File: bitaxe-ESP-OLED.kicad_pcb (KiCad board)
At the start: 2 copper layers, 57.4 x 42 mm, 48 parts, among them J1 SFV30R-4STE1HLF, J2 Conn_01x06, J3 USB_C_Receptacle_USB2.0_16P, Q1 SI2307, SW1 SWITCH-SPST, SW2 SWITCH-SPST, SW3 SWITCH-SPST, SW4 SWITCH-SPST, U1 ESP32_S3R8, U2 RT9080-33GJ5, U3 AP2502KTR-G1, U4 W25Q128JV

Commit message: very rough routing
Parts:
- moved C2 44.0 mm to (146.6, 76.7), turned to 0 degrees
- moved C21 42.5 mm to (161.7, 73.5)
- moved C13 41.6 mm to (161.7, 71.4)
- moved C3 41.3 mm to (142.8, 75.2)
- moved L1 41.2 mm to (150.6, 82.8), turned to 0 degrees
- moved C19 41.1 mm to (166.2, 72.0), turned to -90 degrees
- moved C18 39.0 mm to (165.0, 72.0), turned to 90 degrees
- moved C17 36.9 mm to (164.0, 72.0), turned to -90 degrees
- moved R1 36.1 mm to (150.1, 73.6), turned to 0 degrees
- moved C11 32.3 mm to (150.5, 81.4)
- moved R5 31.8 mm to (134.7, 89.3)
- moved C1 31.2 mm to (146.7, 79.1), turned to 0 degrees
- moved C4 30.9 mm to (150.0, 84.9), turned to 0 degrees
- moved C10 29.2 mm to (165.0, 79.6), turned to 0 degrees
- moved C9 29.2 mm to (171.6, 89.9), turned to -90 degrees
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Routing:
- net /3V3: track 0.00 -> 109.2 mm, vias 0 -> 2
- net /RESET: track 0.00 -> 54.5 mm, vias 0 -> 2
- net /GPIO0: track 0.00 -> 45.9 mm, vias 0 -> 2
- net GND: track 0.00 -> 41.3 mm, vias 0 -> 32
- net /VBUS: track 0.00 -> 39.6 mm
- net /TP_INT: track 0.00 -> 36.3 mm, vias 0 -> 2
- net /+5V: track 0.00 -> 35.7 mm
- net /LCD_RD: track 0.00 -> 24.3 mm, vias 0 -> 2
- net /LCD_WR: track 0.00 -> 23.3 mm, vias 0 -> 2
- net /LCD_DC: track 0.00 -> 22.7 mm, vias 0 -> 2
- net /BAP_RX: track 0.00 -> 22.5 mm, vias 0 -> 1
- net /BAP_TX: track 0.00 -> 22.4 mm, vias 0 -> 1
- net /LCD_CS: track 0.00 -> 22.3 mm, vias 0 -> 2
- net /LCD_RES: track 0.00 -> 20.8 mm
- net /LCD_D7: track 0.00 -> 18.8 mm
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
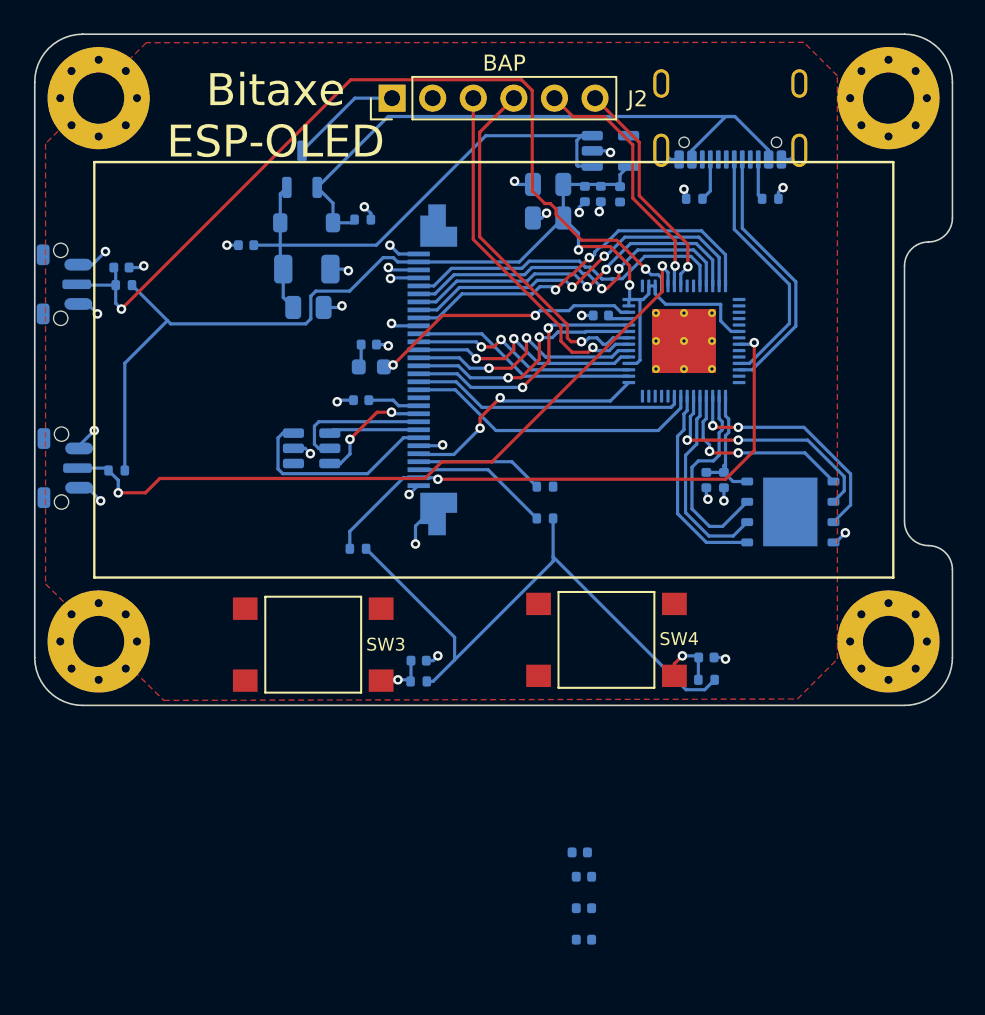
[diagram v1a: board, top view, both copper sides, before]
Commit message: main MCU routing to OLED connector
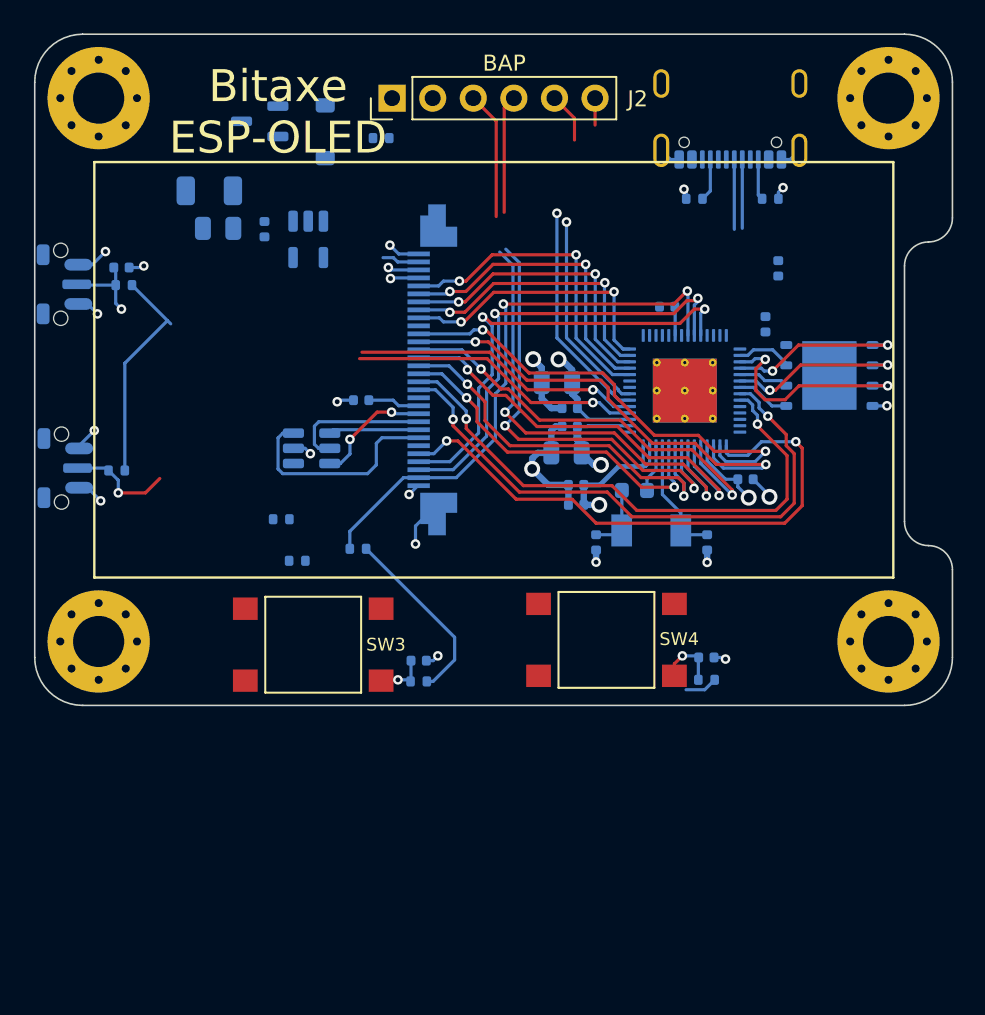
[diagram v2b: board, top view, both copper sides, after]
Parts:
- removed C12: 1uF, Capacitor_SMD:C_0402_1005Metric
- added Y2: 40 MHz, bitaxe:Abracon-ABM3, B.Cu at (168.2, 93.0)
- moved C16 33.3 mm to (163.1, 85.4)
- moved C14 28.2 mm to (163.1, 86.5)
- moved C15 25.2 mm to (163.4, 91.5)
- moved C18 20.0 mm to (174.1, 89.8), turned to 180 degrees
- moved U2 19.7 mm to (146.7, 74.8), turned to -90 degrees
- moved C11 18.9 mm to (164.7, 93.8), turned to 90 degrees
- moved C19 18.4 mm to (163.4, 90.2), turned to 180 degrees
- moved L1 18.2 mm to (167.1, 90.5)
- moved R9 16.5 mm to (145.0, 92.3)
- moved R8 16.2 mm to (146.0, 95.0)
- moved C10 15.7 mm to (171.7, 93.8), turned to 90 degrees
- moved C21 14.7 mm to (162.8, 88.2)
- moved C9 14.0 mm to (176.1, 76.7), turned to 90 degrees
- moved C13 12.4 mm to (162.2, 83.8)
- moved C8 10.1 mm to (175.3, 80.2), turned to 90 degrees
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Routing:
- net /3V3: track 109.2 -> 59.5 mm, vias 2 -> 4
- net /VBUS: track 39.6 -> 0.00 mm
- net /+5V: track 35.7 -> 0.00 mm
- net /RESET: track 54.5 -> 23.6 mm
- net /GPIO0: track 45.9 -> 24.8 mm
- net /TP_RESET: track 15.6 -> 36.4 mm
- net /I2C_SCL: track 8.04 -> 28.6 mm, vias 0 -> 2
- net /I2C_SCK: track 8.65 -> 28.8 mm, vias 0 -> 2
- net /LCD_D6: track 17.2 -> 35.0 mm, vias 0 -> 2
- net /LCD_D7: track 18.8 -> 36.5 mm, vias 0 -> 2
- net /LCD_D1: track 14.3 -> 29.7 mm
- net /LCD_D0: track 14.2 -> 29.2 mm, vias 0 -> 2
- net /BAP_TX: track 22.4 -> 37.3 mm, vias 1 -> 2
- net /XTAL_P: track 17.1 -> 3.03 mm, vias 2 -> 0
- net /BAP_RX: track 22.5 -> 35.8 mm, vias 1 -> 2
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- added copper zone on In1.Cu, net /3V3
- added copper zone on In2.Cu, net GND
- removed copper zone on F.Cu, net GND
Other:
- copper layers 2 -> 4

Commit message: finish most of the routing
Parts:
- J2: moved to B.Cu
- moved C9 24.7 mm to (151.4, 76.8), turned to -90 degrees
- moved C1 5.20 mm to (144.1, 69.9), turned to 90 degrees
- moved R8 4.34 mm to (147.8, 91.0), turned to 0 degrees
- moved Q1 4.16 mm to (147.8, 67.2), turned to 90 degrees
- moved R7 3.04 mm to (172.3, 99.5)
- moved R6 2.85 mm to (153.6, 99.7)
- moved R9 2.80 mm to (147.8, 92.2), turned to 0 degrees
- moved D2 2.75 mm to (147.7, 70.8), turned to 0 degrees
- moved C2 2.59 mm to (141.3, 69.3), turned to 90 degrees
- moved C3 2.55 mm to (142.1, 72.5), turned to 180 degrees
- moved R10 2.10 mm to (147.8, 93.5), turned to 0 degrees
- moved C4 1.79 mm to (151.7, 84.2), turned to -90 degrees
- moved U2 1.65 mm to (145.1, 75.0)
- moved C5 1.58 mm to (134.7, 78.2), turned to -90 degrees
- moved R4 1.55 mm to (136.7, 77.7)
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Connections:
- C4 pad 2: /LEDA -> /3V3
- C9 pad 1: /VDD_SPI -> /3V3
- J1 pad 20: /LEDA -> /3V3
- J1 pad 21: /LEDK1 -> /LEDK4
- J1 pad 22: /LEDK2 -> /LEDK3
- J1 pad 23: /LEDK3 -> /LEDK2
- J1 pad 24: /LEDK4 -> /LEDK1
- U1 pad 18: unconnected-(U1-GPIO13-Pad18) -> /UI2
- U1 pad 19: unconnected-(U1-GPIO14-Pad19) -> /UI1
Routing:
- net /UI2: track 3.93 -> 50.2 mm
- net /UI1: track 3.21 -> 47.8 mm
- net /VBUS: track 0.00 -> 36.8 mm, vias 0 -> 3
- net GND: track 41.3 -> 68.7 mm, vias 22 -> 30
- net /GPIO0: track 24.8 -> 43.3 mm
- net /+5V: track 0.00 -> 15.7 mm
- net /RESET: track 23.6 -> 39.2 mm
- net /3V3: track 59.5 -> 47.4 mm, vias 4 -> 14
- net /USB_DP: track 4.30 -> 14.3 mm
- net /USB_DM: track 4.37 -> 13.6 mm
- net /I2C_SCK: track 28.8 -> 36.7 mm
- net /GPIO2: track 14.4 -> 21.4 mm
- net /I2C_SCL: track 28.6 -> 34.8 mm
- net /LEDK4: track 13.7 -> 8.31 mm
- net /GPIO1: track 17.1 -> 21.6 mm
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
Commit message: Finish up routing
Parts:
- removed Y2: 40 MHz, bitaxe:Abracon-ABM3
- added Y1: 40MHz, bitaxe:RH100-oscillator, B.Cu at (169.2, 93.8)
- U1: footprint Package_DFN_QFN:QFN-56-1EP_7x7mm_P0.4mm_EP4x4mm_ThermalVias -> bitaxe:QFN-56-1EP_7x7mm_P0.4mm_EP4x4mm_ThermalVias
- moved C11 1.74 mm to (166.1, 94.9), turned to 0 degrees
- moved L1 1.37 mm to (166.6, 91.8), turned to 90 degrees
- moved J3 0.46 mm to (173.1, 65.7)
- moved C10 0.38 mm to (171.7, 93.4)
- moved SW4 0.30 mm to (165.3, 100.2)
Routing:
- net GND: track 68.7 -> 72.0 mm, vias 30 -> 31
- net /XTAL_P: track 3.03 -> 4.48 mm
- net /VBUS: track 36.8 -> 37.7 mm
- net /LCD_D3: track 26.5 -> 27.2 mm
- net /USB_DM: track 13.6 -> 14.2 mm
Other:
- board text added: "BOOT"
- board text added: "RES"
- board text added: "USER1"
- board text added: "USER2"

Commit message: commit version 0.1
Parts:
- added J3: TC2030-IDC, Connector:Tag-Connect_TC2030-IDC-NL_2x03_P1.27mm_Vertical, F.Cu at (175.1, 99.9)
- added TP1: TestPoint, TestPoint:TestPoint_Pad_D1.0mm, B.Cu at (158.2, 70.6)
- added TP10: TestPoint, TestPoint:TestPoint_Pad_D1.0mm, B.Cu at (141.4, 80.3)
- added TP11: TestPoint, TestPoint:TestPoint_Pad_D1.0mm, B.Cu at (137.9, 70.9)
- added TP13: TestPoint, TestPoint:TestPoint_Pad_D1.0mm, B.Cu at (142.9, 88.8)
- added TP2: TestPoint, TestPoint:TestPoint_Pad_D1.0mm, B.Cu at (160.9, 70.7)
- added TP3: TestPoint, TestPoint:TestPoint_Pad_D1.0mm, F.Cu at (162.1, 68.8)
- added TP4: TestPoint, TestPoint:TestPoint_Pad_D1.0mm, F.Cu at (163.4, 71.2)
- added TP5: TestPoint, TestPoint:TestPoint_Pad_D1.0mm, B.Cu at (136.2, 75.0)
- added TP6: TestPoint, TestPoint:TestPoint_Pad_D1.0mm, F.Cu at (175.8, 96.8)
- added TP7: TestPoint, TestPoint:TestPoint_Pad_D1.0mm, F.Cu at (173.2, 96.8)
- added TP8: TestPoint, TestPoint:TestPoint_Pad_D1.0mm, B.Cu at (146.9, 80.4)
- added TP9: TestPoint, TestPoint:TestPoint_Pad_D1.0mm, B.Cu at (135.2, 91.1)
- moved R4 16.7 mm to (155.8, 101.5), turned to 0 degrees
- moved C3 16.6 mm to (155.8, 100.0), turned to 180 degrees
- moved R2 3.81 mm to (155.8, 96.5)
- moved C2 3.81 mm to (155.7, 98.0)
- renumbered C5 to C1, C18 to C10, C19 to C11, C16 to C12, C15 to C13, C2 to C14, C1 to C15, C3 to C16, C9 to C17, C4 to C18, C8 to C19, C6 to C2, C7 to C3, C21 to C4, C14 to C5, C17 to C6, C10 to C7, C11 to C8, C13 to C9, D2 to D1, J2 to J1, J3 to J2, J1 to J4, R4 to R1, R6 to R2, R5 to R3, R7 to R4, R2 to R5, R3 to R6, R1 to R7, SW3 to SW2, SW2 to SW3, U2 to U1, U1 to U2
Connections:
- U2 pad 15: unconnected-(U1-GPIO10-Pad15) -> /BAP_TX
- U2 pad 16: unconnected-(U1-GPIO11-Pad16) -> /BAP_RX
- U2 pad 27: unconnected-(U1-GPIO21-Pad27) -> /TP_RESET
- U2 pad 43: /TP_RESET -> /LCD_BLK
- U2 pad 49: /BAP_TX -> /P_TX
- U2 pad 50: /BAP_RX -> /P_RX
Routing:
- net /RESET: track 39.2 -> 98.5 mm
- net /GPIO0: track 43.3 -> 102.6 mm
- net /LCD_BLK: track 0.00 -> 48.4 mm, vias 0 -> 2
- net /BAP_TX: track 40.0 -> 20.9 mm
- net /BAP_RX: track 38.1 -> 19.4 mm
- net /P_TX: track 0.00 -> 15.8 mm, vias 0 -> 1
- net /P_RX: track 0.00 -> 15.2 mm, vias 0 -> 1
- net GND: track 72.0 -> 81.3 mm
- net /TP_RESET: track 35.8 -> 41.9 mm
- net /UI2: track 50.5 -> 55.6 mm
- net /3V3: track 47.4 -> 52.4 mm, vias 14 -> 15
- net /+5V: track 15.7 -> 19.2 mm
- net /TP_INT: track 40.0 -> 40.7 mm
- net /I2C_SCK: track 36.7 -> 37.4 mm
- net /I2C_SCL: track 34.8 -> 35.5 mm
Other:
- board text added: "+5V"
- board text added: "3.3V"
- board text added: "GND"
- board text added: "V0.1"

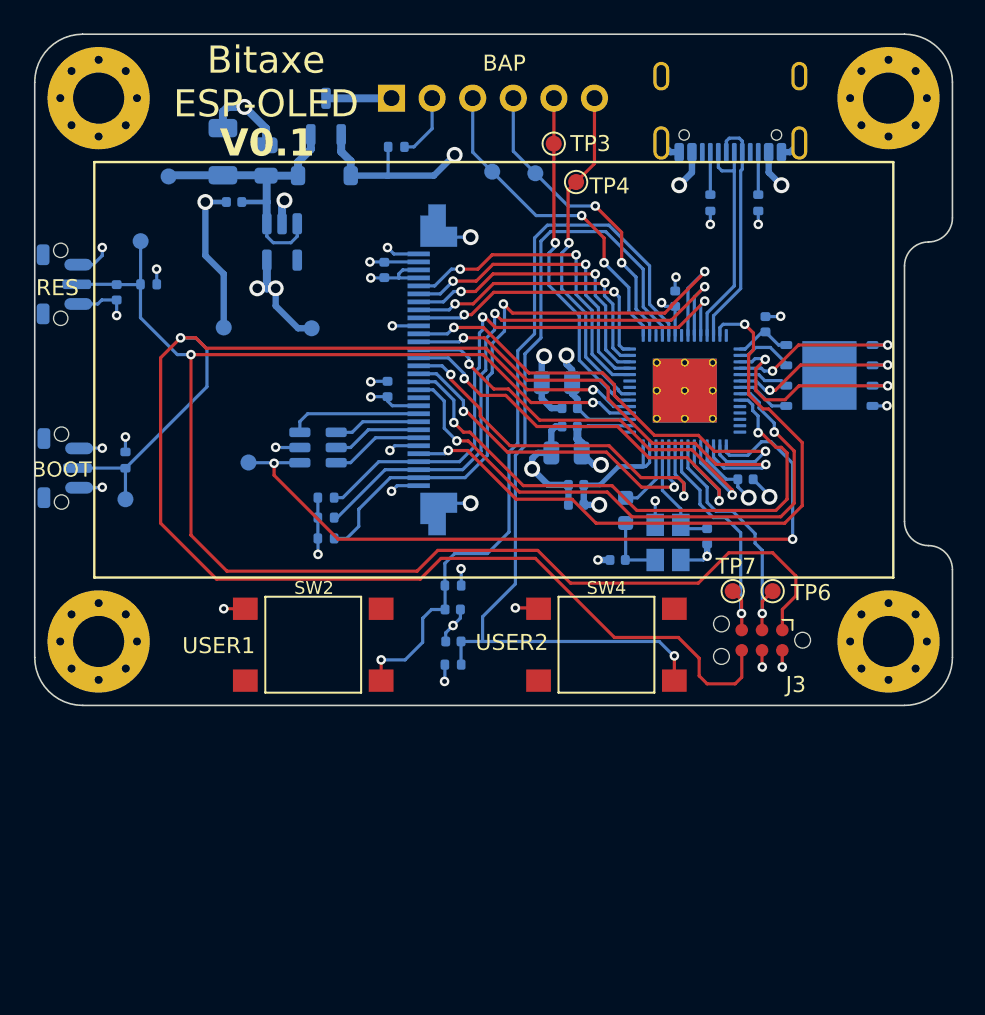
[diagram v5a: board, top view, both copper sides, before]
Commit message: reverse BAP port
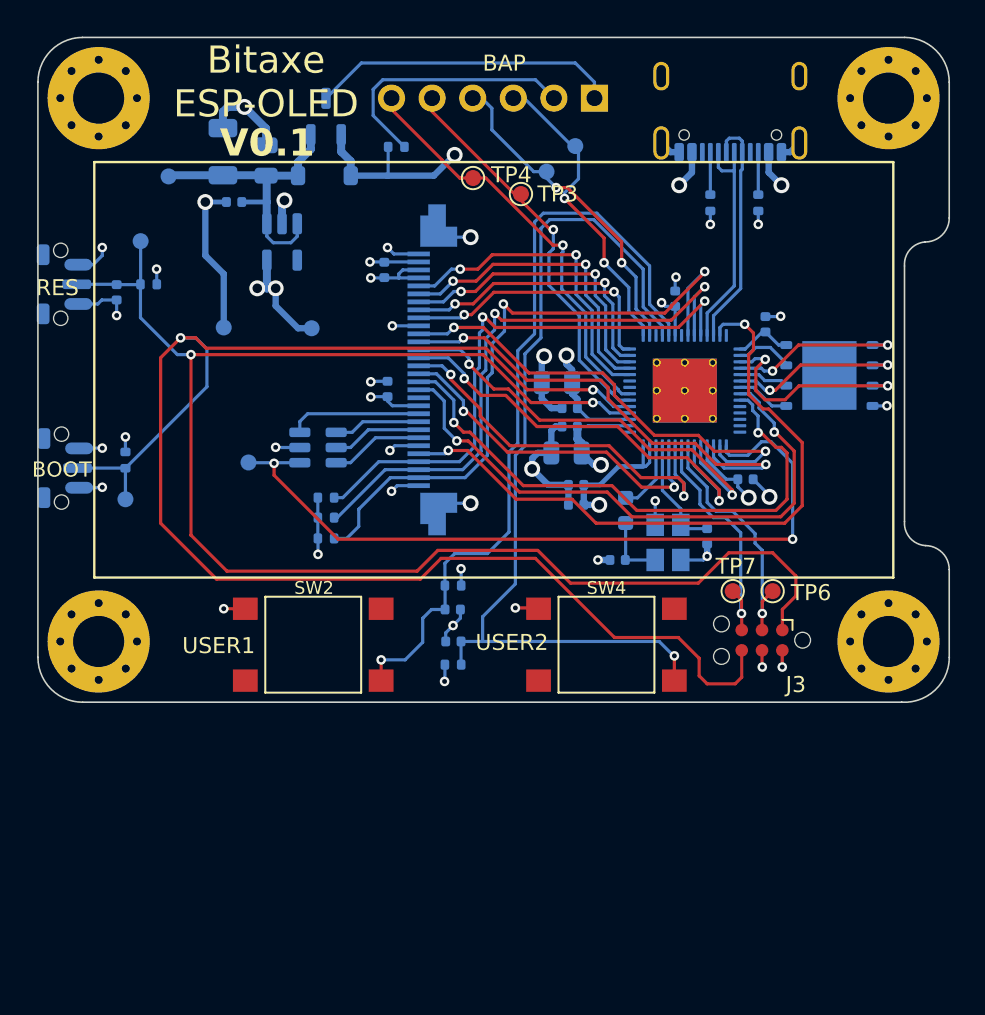
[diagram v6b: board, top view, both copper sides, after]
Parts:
- moved J1 12.7 mm to (164.6, 66.0), turned to 90 degrees
- moved TP4 6.45 mm to (157.0, 71.0)
- moved TP1 5.44 mm to (163.4, 69.0)
- moved TP3 3.76 mm to (160.0, 72.0)
- moved TP2 0.71 mm to (161.6, 70.6)
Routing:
- net /5V_BAP: track 4.11 -> 19.2 mm
- net GND: track 81.3 -> 93.6 mm
- net /GPIO2: track 21.4 -> 26.4 mm
- net /GPIO1: track 21.6 -> 24.8 mm
- net /BAP_TX: track 20.9 -> 19.3 mm
- net /UI1: track 47.7 -> 48.9 mm
- net /BAP_RX: track 19.4 -> 20.5 mm
- net /UI2: track 55.6 -> 56.7 mm
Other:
- board size 57.4 x 42 mm -> 57 x 41.6 mm
